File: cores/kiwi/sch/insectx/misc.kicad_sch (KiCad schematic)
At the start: 21 parts, among them SW1 SW_DIP_x02, U11 74LS04, U12 74LS08, U17 74LS74, U22 74LS244_Split, U29 74LS32, U48 74LS14, U49 74LS161

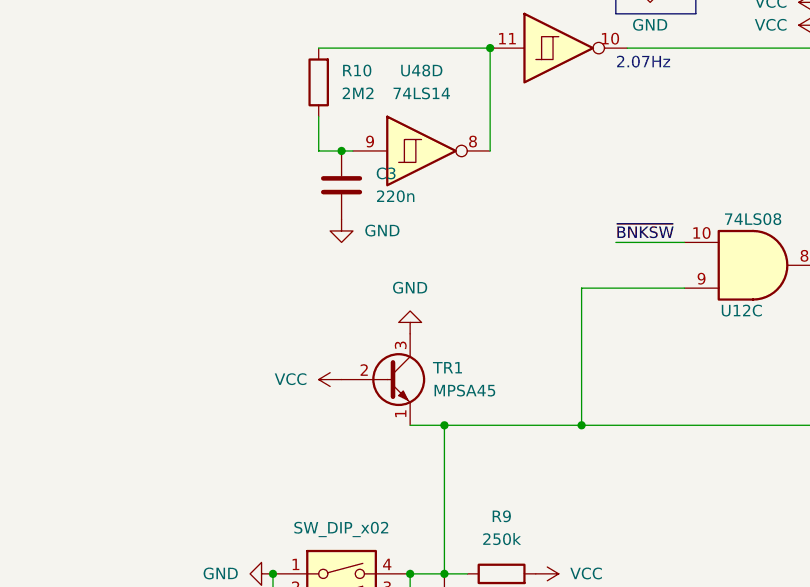
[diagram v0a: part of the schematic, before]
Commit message: Updated schematics according to: [insectx] schematic signals #22
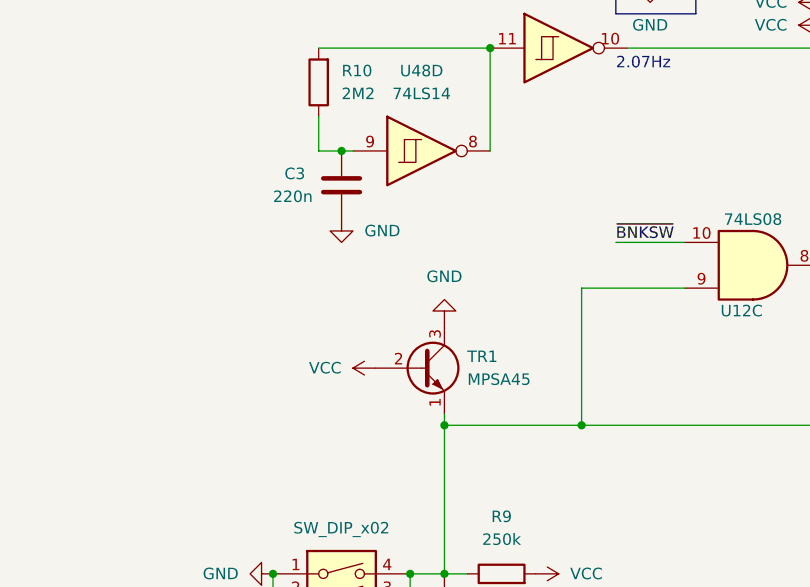
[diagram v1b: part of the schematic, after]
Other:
- moved on the sheet: TR1
